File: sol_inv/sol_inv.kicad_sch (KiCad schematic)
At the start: 0 parts

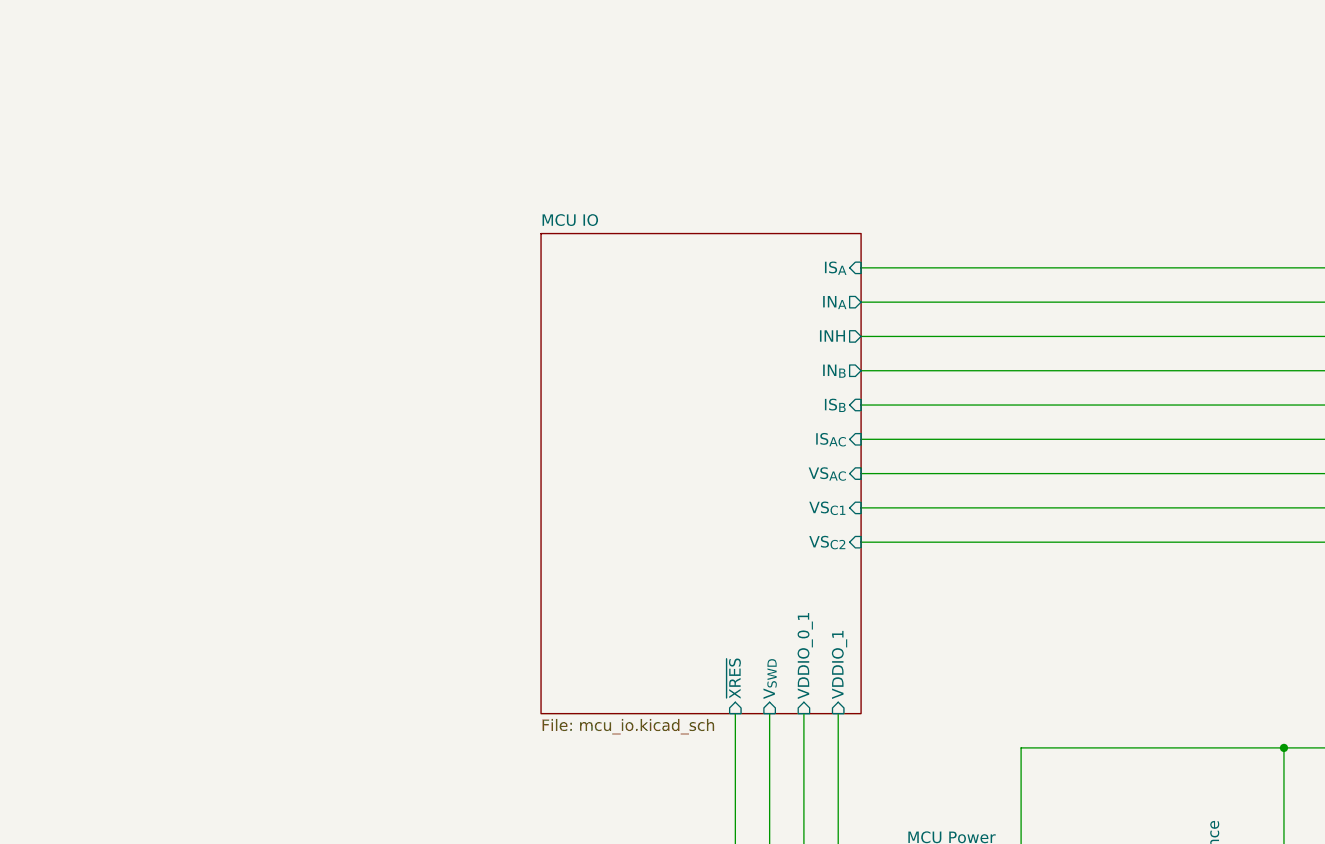
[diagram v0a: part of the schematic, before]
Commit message: v0.2 components change + reference to providers
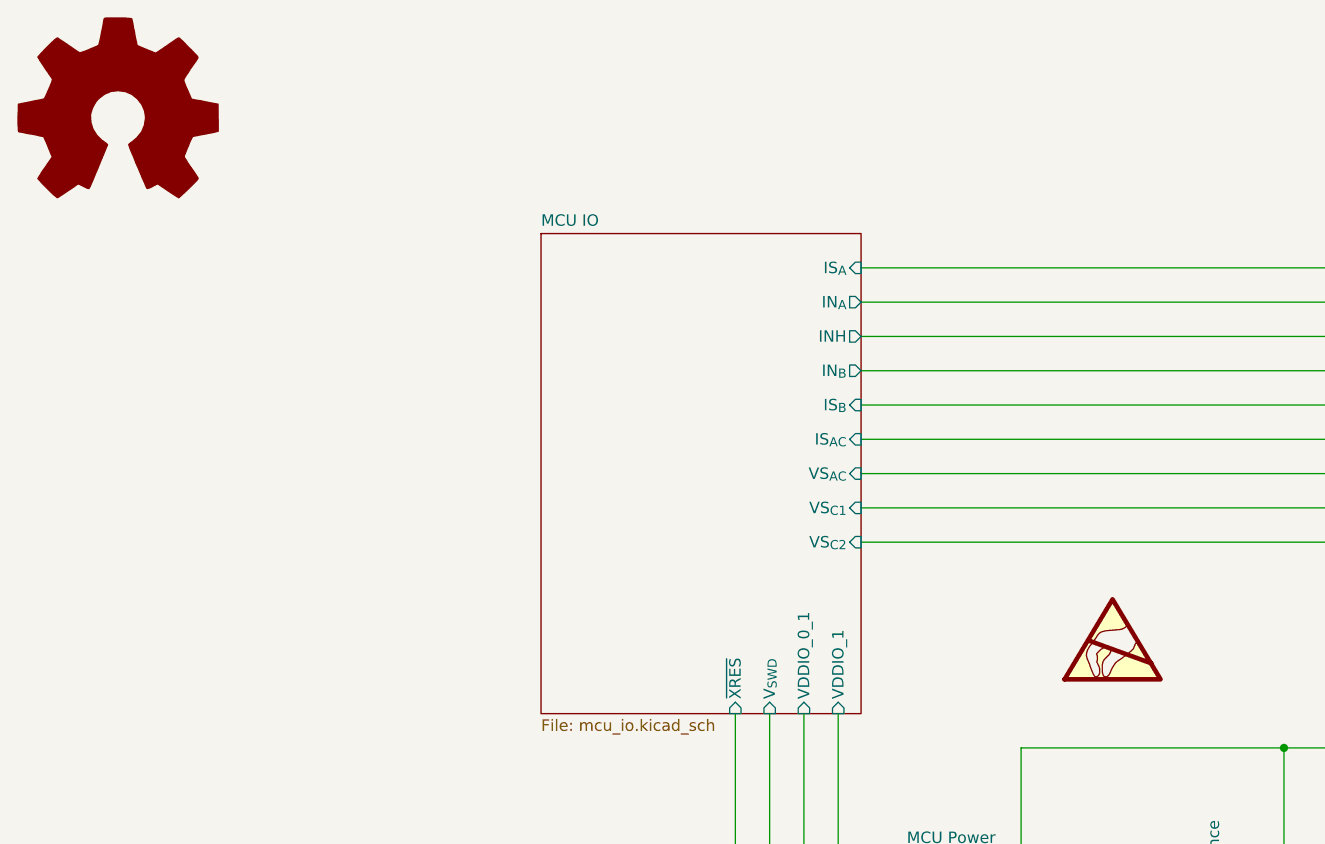
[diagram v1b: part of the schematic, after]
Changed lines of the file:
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@@
 	(title_block
 		(title "PCB Overview")
-		(date "2025-03-13")
-		(rev "0.1")
+		(date "2025-04-10")
+		(rev "0.2")
 		(company "Cezar-Octavian Bontaș")
 	)
@@
 		)
 	)
+	(symbol
+		(lib_id "Graphic:SYM_ESD_Large")
+		(at 149.86 90.17 0)
+		(unit 1)
+		(exclude_from_sim yes)
+		(in_bom no)
+		(on_board no)
+		(dnp no)
+		(fields_autoplaced yes)
+		(property "Reference" "#SYM2"
+			(at 149.86 85.09 0)
+			(effects
+				(font
+					(size 1.27 1.27)
+				)
+				(hide yes)
+			)
+		)
+		(property "Value" "SYM_ESD_Large"
+			(at 149.86 96.52 0)
+			(effects
+				(font
+					(size 1.27 1.27)
+				)
+				(hide yes)
+			)
+		)
+		(property "Footprint" ""
+			(at 149.733 90.932 0)
+			(effects
+				(font
+					(size 1.27 1.27)
+				)
+				(hide yes)
+			)
+		)
+		(property "Datasheet" "~"
+			(at 149.733 90.932 0)
+			(effects
+				(font
+					(size 1.27 1.27)
+				)
+				(hide yes)
+			)
+		)
+		(property "Description" "ESD warning/\"Do not touch\" symbol, large"
+			(at 149.86 90.17 0)
+			(effects
+				(font
+					(size 1.27 1.27)
+				)
+				(hide yes)
+			)
+		)
+		(instances
+			(project ""
+				(path "/c5b733d3-d844-4c5a-a928-539beea9cfbc"
+					(reference "#SYM2")
+					(unit 1)
+				)
+			)
+		)
+	)
+	(symbol
+		(lib_id "Graphic:Logo_Open_Hardware_Large")
+		(at 39.37 33.02 0)
+		(unit 1)
+		(exclude_from_sim yes)
+		(in_bom no)
+		(on_board no)
+		(dnp no)
+		(fields_autoplaced yes)
+		(property "Reference" "#SYM1"
+			(at 39.37 20.32 0)
+			(effects
+				(font
+					(size 1.27 1.27)
+				)
+				(hide yes)
+			)
+		)
+		(property "Value" "Logo_Open_Hardware_Large"
+			(at 39.37 43.18 0)
+			(effects
+				(font
+					(size 1.27 1.27)
+				)
+				(hide yes)
+			)
+		)
+		(property "Footprint" ""
+			(at 39.37 33.02 0)
+			(effects
+				(font
+					(size 1.27 1.27)
+				)
+				(hide yes)
+			)
+		)
+		(property "Datasheet" "~"
+			(at 39.37 33.02 0)
+			(effects
+				(font
+					(size 1.27 1.27)
+				)
+				(hide yes)
+			)
+		)
+		(property "Description" "Open Hardware logo, large"
+			(at 39.37 33.02 0)
+			(effects
+				(font
+					(size 1.27 1.27)
+				)
+				(hide yes)
+			)
+		)
+		(instances
+			(project ""
+				(path "/c5b733d3-d844-4c5a-a928-539beea9cfbc"
+					(reference "#SYM1")
+					(unit 1)
+				)
+			)
+		)
+	)

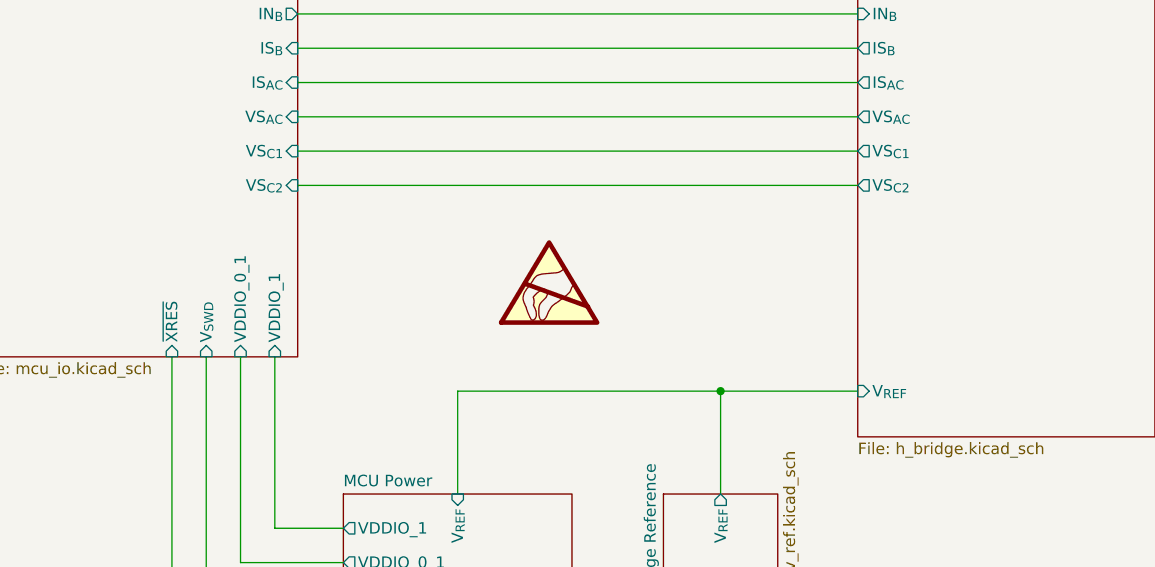
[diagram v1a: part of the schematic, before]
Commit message: initial component placement
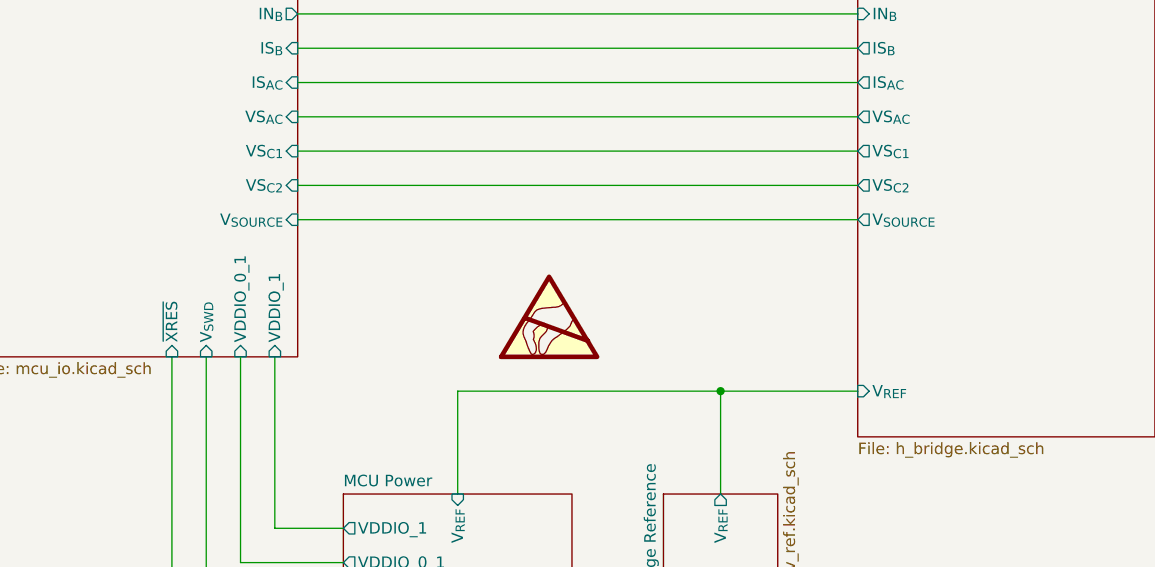
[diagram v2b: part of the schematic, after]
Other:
- sheet H-Bridge ports: added V_{SOURCE}; removed none
- sheet MCU IO ports: added V_{SOURCE}; removed none
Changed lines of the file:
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@@
 	(title_block
 		(title "PCB Overview")
-		(date "2025-04-10")
-		(rev "0.2")
+		(date "2025-04-24")
+		(rev "0.2.1")
 		(company "Cezar-Octavian Bontaș")
 	)
@@
 	(wire
 		(pts
+			(xy 121.92 83.82) (xy 184.15 83.82)
+		)
+		(stroke
+			(width 0)
+			(type default)
+		)
+	)
+	(wire
+		(pts
 			(xy 111.76 125.73) (xy 127 125.73)
 		)
@@
 	(symbol
 		(lib_id "Graphic:SYM_ESD_Large")
-		(at 149.86 90.17 0)
+		(at 149.86 93.98 0)
 		(unit 1)
-		(exclude_from_sim yes)
+		(exclude_from_sim no)
 		(in_bom no)
 		(on_board no)
@@
 		(fields_autoplaced yes)
 		(property "Reference" "#SYM2"
-			(at 149.86 85.09 0)
+			(at 149.86 88.9 0)
 			(effects
 				(font
@@
 		)
 		(property "Value" "SYM_ESD_Large"
-			(at 149.86 96.52 0)
+			(at 149.86 100.33 0)
 			(effects
 				(font
@@
 		)
 		(property "Footprint" ""
-			(at 149.733 90.932 0)
+			(at 149.733 94.742 0)
 			(effects
 				(font
@@
 		)
 		(property "Datasheet" "~"
-			(at 149.733 90.932 0)
+			(at 149.733 94.742 0)
 			(effects
 				(font
@@
 		)
 		(property "Description" "ESD warning/\"Do not touch\" symbol, large"
-			(at 149.86 90.17 0)
+			(at 149.86 93.98 0)
 			(effects
 				(font
@@
 		(at 39.37 33.02 0)
 		(unit 1)
-		(exclude_from_sim yes)
+		(exclude_from_sim no)
 		(in_bom no)
 		(on_board no)
@@
 			)
 		)
+		(pin "V_{SOURCE}" output
+			(at 184.15 83.82 180)
+			(effects
+				(font
+					(size 1.27 1.27)
+				)
+				(justify left)
+			)
+		)
 		(instances
 			(project "sol_inv"
@@
 			)
 		)
+		(pin "V_{SOURCE}" input
+			(at 121.92 83.82 0)
+			(effects
+				(font
+					(size 1.27 1.27)
+				)
+				(justify right)
+			)
+		)

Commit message: v0.4 fixed mcu ldo part, production testing
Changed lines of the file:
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@@
 	(title_block
 		(title "PCB Overview")
-		(date "2025-05-26")
-		(rev "0.3.1")
+		(date "2025-07-29")
+		(rev "0.4")
 		(company "Cezar-Octavian Bontaș")
 	)
@@
 	)
 	(sheet
-		(at 137.16 163.83)
+		(at 184.15 118.11)
 		(size 27.94 15.24)
 		(exclude_from_sim no)
@@
 		)
 		(property "Sheetname" "Power Source"
-			(at 137.16 163.1184 0)
+			(at 184.15 117.3984 0)
 			(effects
 				(font
@@
 		)
 		(property "Sheetfile" "pwr_pcb.kicad_sch"
-			(at 137.16 179.6546 0)
-			(effects
-				(font
+			(at 184.15 133.9346 0)
+			(effects
+				(font
